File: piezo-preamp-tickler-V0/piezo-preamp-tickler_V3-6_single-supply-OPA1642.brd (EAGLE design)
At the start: 100.3 x 20.1 mm, 58 parts, among them IC1 OPA1642, IC2 DMN2400, IC3 BQ21040, IC4 BQ297X, IC5 SC4503, IC6 TPS7A49, J1 HEADPHONES, J2 PHONE, J3 Mixer, J5 Battery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

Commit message: Add files via upload
DRC issues fixed for previous changes
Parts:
- moved R19 2.51 mm to (51.9, 14.0)
- moved R17 2.20 mm to (52.0, 11.0)
- moved CN1 0.32 mm to (38.1, 16.7)
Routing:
- net N$30: track 120.0 -> 115.6 mm
- net V+: track 114.5 -> 117.4 mm
- net N$28: track 63.3 -> 65.4 mm
- net N$17: track 100.4 -> 101.9 mm
- net GND: track 177.1 -> 178.5 mm
- net N$29: track 53.2 -> 52.0 mm

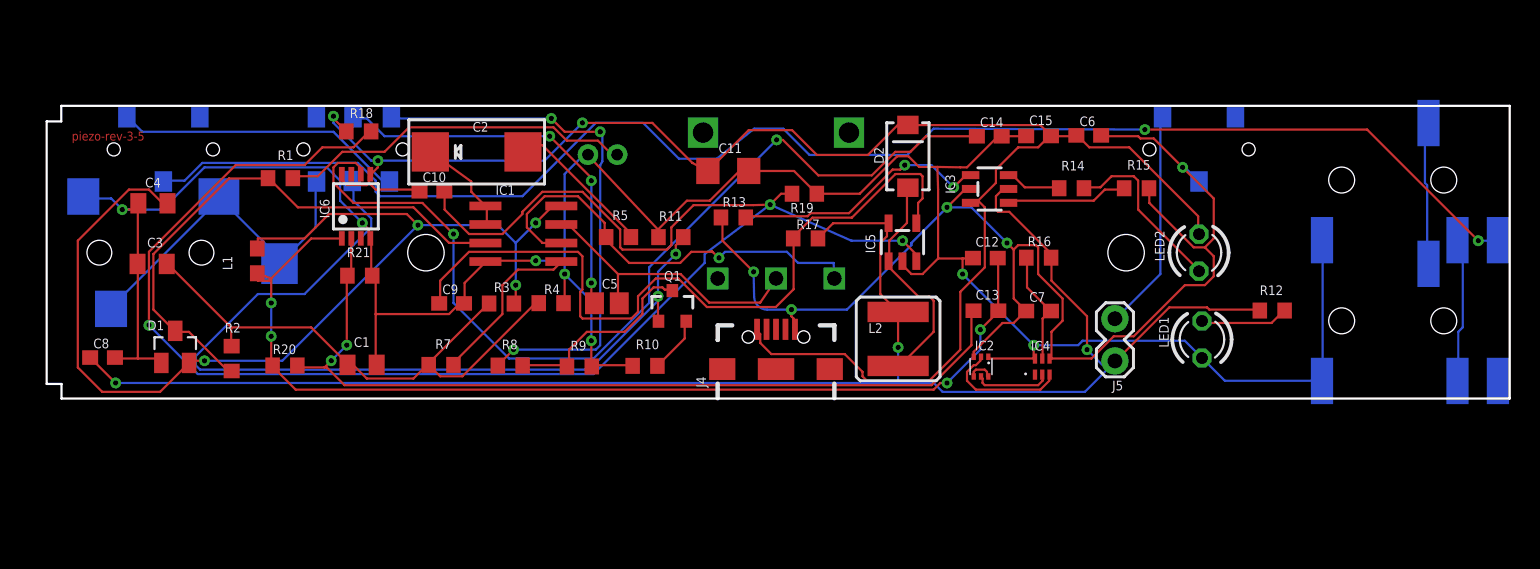
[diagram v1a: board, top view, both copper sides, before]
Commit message: issues 14 and 17 resolved
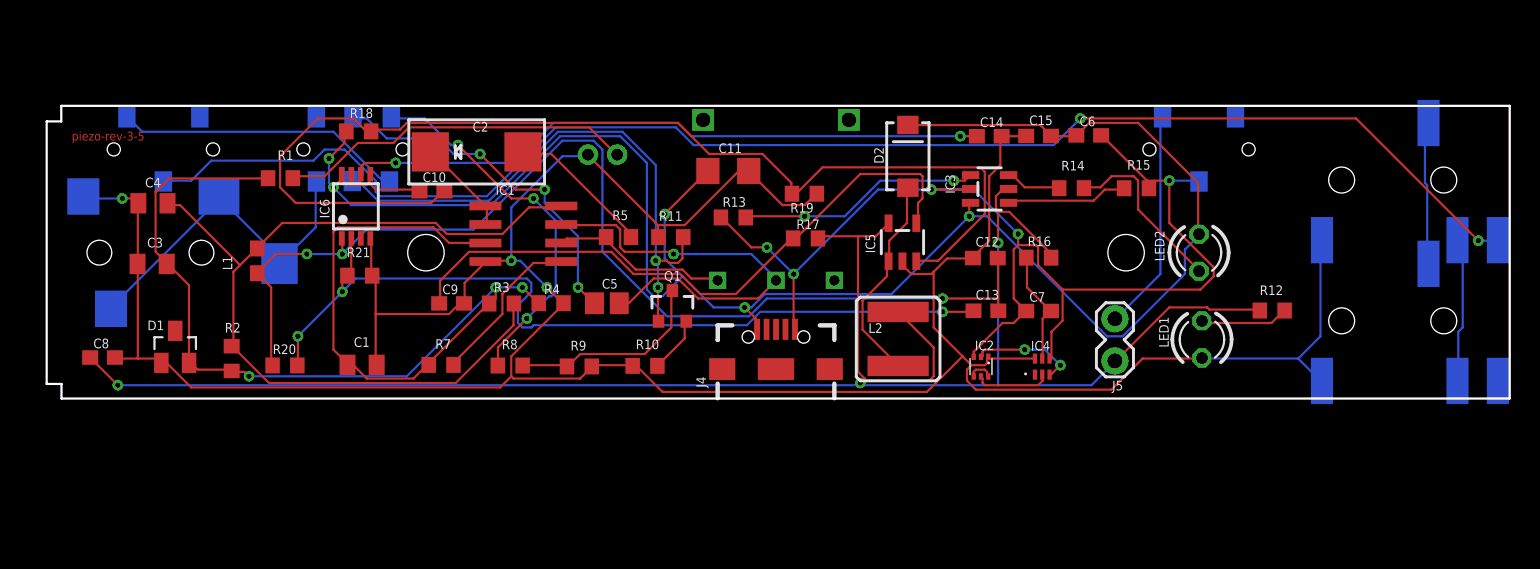
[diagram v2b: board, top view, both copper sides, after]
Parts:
- removed R6: 50K, CMU-ArtFab:THUMBPOT14MM
- added U$1: PIEZO-PREAMP-TICKLER_V3-5_SINGLE-SUPPLY-OPA1642_50K_DIAL_POT, custom_packages:PIEZO-PREAMP-TICKLER_V3-5_SINGLE-SUPPLY-OPA1642_50K_DIAL_POT
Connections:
- removed net N$23: C1.1, C3.1, R2.1, R3.1, R4.2, R7.2
- removed net N$25: C4.1, D1.2, IC1.8, L1.2, R3.2
- removed net N$9: D1.3, IC1.3, R1.2, R2.2
- new net N$1: C1.1, C3.1, D1.2, IC1.3, R1.2, R2.2, R3.1, R4.2, R7.2
- new net N$8: C4.1, IC1.8, L1.2, R2.1, R3.2
- net N$6: now also U$1.2; no longer R6.P$2
- net N$7: now also U$1.1; no longer R6.P$1
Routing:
- net N$1: track 0.00 -> 82.3 mm, vias 0 -> 3
- net N$25: track 73.7 -> 0.00 mm, vias 4 -> 0
- net N$8: track 0.00 -> 60.4 mm
- net N$30: track 115.6 -> 76.4 mm, vias 3 -> 0
- net N$23: track 38.9 -> 0.00 mm
- net N$9: track 37.7 -> 0.00 mm
- net GND: track 178.5 -> 204.9 mm, vias 7 -> 3
- net SELECT: track 60.6 -> 38.6 mm
- net N$28: track 65.4 -> 44.4 mm
- net N$7: track 30.0 -> 12.2 mm, vias 1 -> 0
- net V+: track 117.4 -> 132.9 mm, vias 3 -> 5
- net N$11: track 37.0 -> 25.9 mm
- net VBAT: track 118.1 -> 128.7 mm
- net N$6: track 19.9 -> 29.6 mm, vias 0 -> 1
- net N$29: track 52.0 -> 43.7 mm
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
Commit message: Custom device added for 50K pot
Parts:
- U$1: device custom_packages:PIEZO-PREAMP-TICKLER_V3-5_SINGLE-SUPPLY-OPA1642_50K_DIAL_POT -> CMU-ArtFab:PIEZO-PREAMP-TICKLER_V3-5_SINGLE-SUPPLY-OPA1642_50K_DIAL_POT
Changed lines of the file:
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@@
 <attribute name="VALUE" x="69.175" y="17.175" size="0.6604" layer="27" font="vector" ratio="15" rot="R180"/>
 </element>
-<element name="U$1" library="custom_packages" package="PIEZO-PREAMP-TICKLER_V3-5_SINGLE-SUPPLY-OPA1642_50K_DIAL_POT" value="PIEZO-PREAMP-TICKLER_V3-5_SINGLE-SUPPLY-OPA1642_50K_DIAL_POT" x="50" y="16.1"/>
+<element name="U$1" library="CMU-ArtFab" package="PIEZO-PREAMP-TICKLER_V3-5_SINGLE-SUPPLY-OPA1642_50K_DIAL_POT" value="PIEZO-PREAMP-TICKLER_V3-5_SINGLE-SUPPLY-OPA1642_50K_DIAL_POT" x="50" y="16.1"/>
 </elements>
 <signals>

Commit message: issue #18 solved
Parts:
- R20: value 91.2k -> 100k
- R21: value 100k -> 11k
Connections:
- net N$12: now also SW1.6; no longer SW1.3
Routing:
- net V+: track 132.9 -> 99.0 mm
- net N$19: track 19.8 -> 43.0 mm
- net N$17: track 100.9 -> 119.0 mm
- net GND2: track 80.9 -> 98.4 mm, vias 5 -> 3
- net N$1: track 82.3 -> 66.1 mm
- net N$28: track 44.4 -> 58.8 mm, vias 2 -> 0
- net N$30: track 76.4 -> 64.6 mm, vias 0 -> 2
- net GND: track 204.9 -> 213.0 mm, vias 3 -> 2
- net N$6: track 29.6 -> 22.0 mm, vias 1 -> 0
- net +12V: track 75.7 -> 68.3 mm, vias 3 -> 2
- net SELECT: track 38.6 -> 31.3 mm, vias 2 -> 4
- net N$11: track 25.9 -> 29.8 mm
- net VBAT: track 128.7 -> 132.0 mm
- net N$12: track 23.8 -> 26.3 mm
- net N$26: track 58.6 -> 56.2 mm, vias 3 -> 2
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
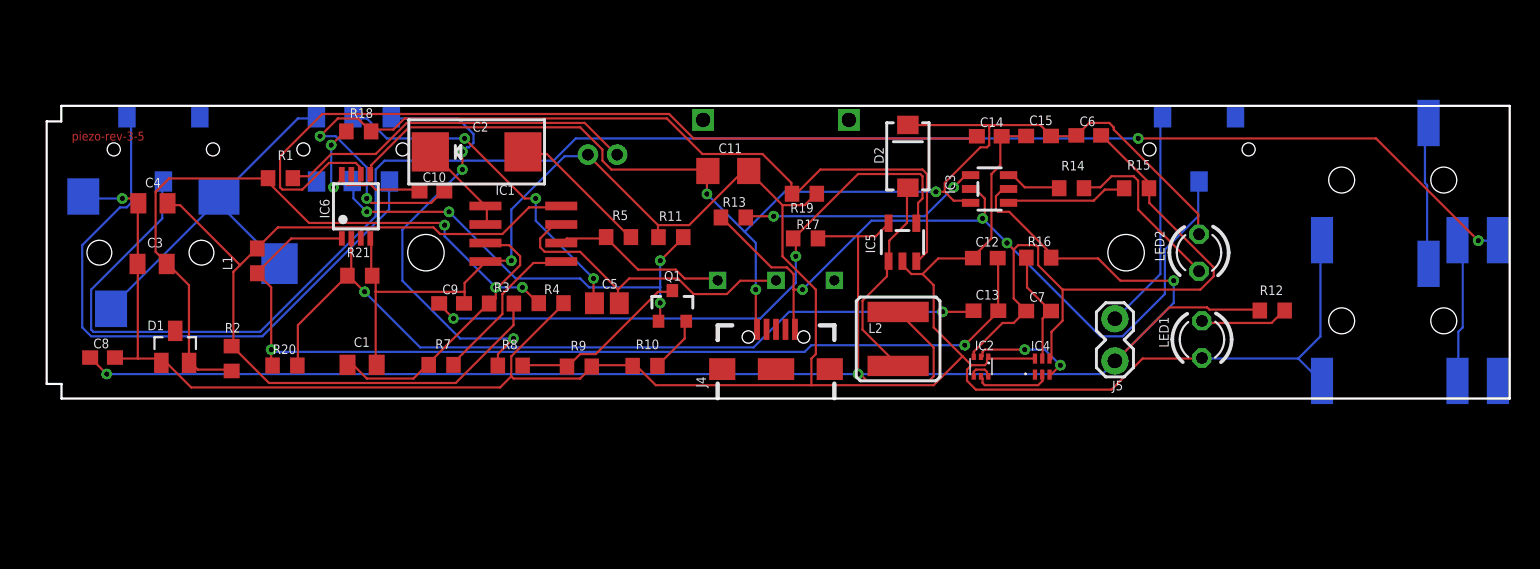
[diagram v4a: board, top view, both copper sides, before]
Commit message: Issues 17 and 19 fixed
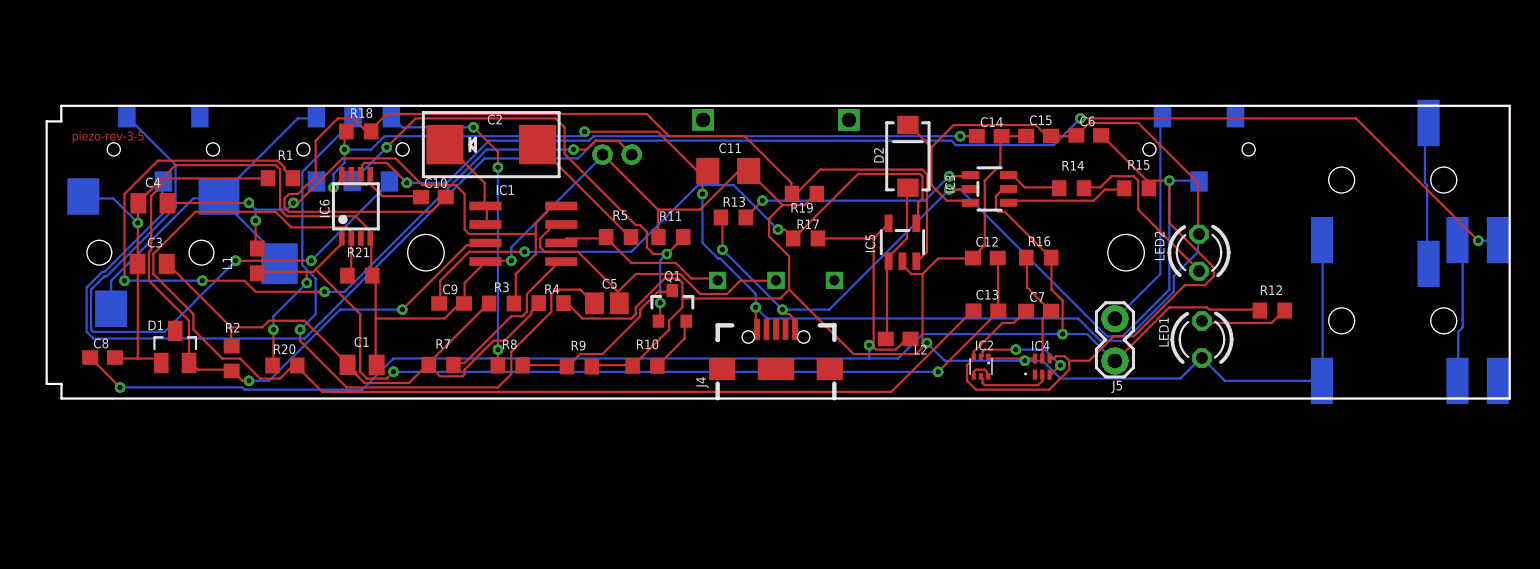
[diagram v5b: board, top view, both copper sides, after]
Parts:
- L2: device SparkFun-Passives:CR54 -> SparkFun-Passives:0603
- moved C2 1.12 mm to (30.5, 17.4)
- moved CN1 1.00 mm to (39.1, 16.7)
- moved C10 0.41 mm to (26.5, 13.8)
- turned L2 to 180 degrees
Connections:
- new net N$9: C1.1, C3.1, R2.1, R3.1, R4.2, R7.2
- net N$1: no longer C1.1, C3.1, R3.1, R4.2, R7.2
- net N$32: now also L2.2; no longer L2.P$2
- net N$8: no longer R2.1
- net VBAT: now also L2.1; no longer L2.P$1
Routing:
- net N$9: track 0.00 -> 39.9 mm
- net N$2: track 24.7 -> 58.8 mm, vias 0 -> 4
- net N$26: track 56.2 -> 83.1 mm, vias 2 -> 0
- net V+: track 99.0 -> 120.5 mm
- net N$1: track 66.1 -> 45.9 mm, vias 3 -> 2
- net N$16: track 23.7 -> 43.9 mm, vias 3 -> 1
- net N$8: track 60.1 -> 41.6 mm, vias 0 -> 3
- net VBAT: track 132.0 -> 114.6 mm
- net N$28: track 58.8 -> 44.8 mm, vias 0 -> 2
- net GND: track 213.0 -> 200.7 mm, vias 2 -> 4
- net N$11: track 29.8 -> 22.9 mm
- net N$30: track 64.6 -> 70.7 mm, vias 2 -> 0
- net SELECT: track 31.3 -> 35.4 mm, vias 4 -> 3
- net +12V: track 68.3 -> 72.3 mm, vias 2 -> 4
- net N$32: track 14.5 -> 11.0 mm
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
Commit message: Bug in issue #23 fixed
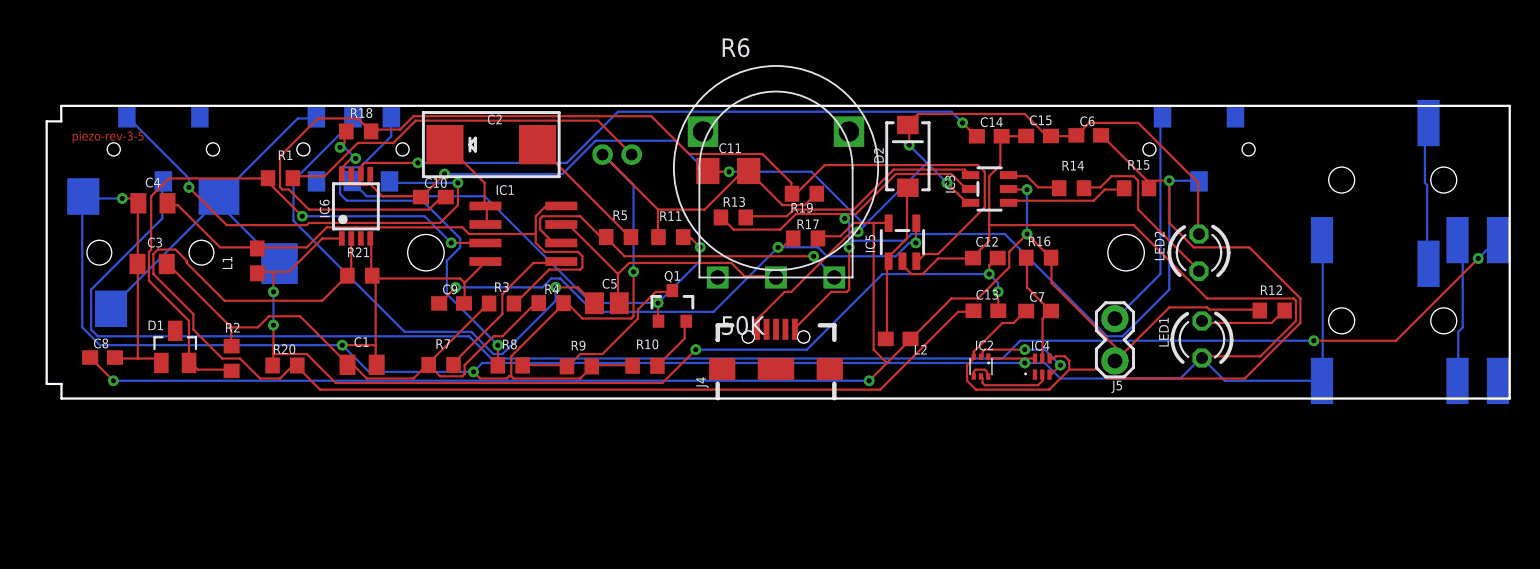
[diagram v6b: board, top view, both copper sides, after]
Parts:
- removed U$1: PIEZO-PREAMP-TICKLER_V3-5_SINGLE-SUPPLY-OPA1642_50K_DIAL_POT, CMU-ArtFab:PIEZO-PREAMP-TICKLER_V3-5_SINGLE-SUPPLY-OPA1642_50K_DIAL_POT
- added R6: 50K, CMU-ArtFab:THUMBPOT14MM
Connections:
- net N$6: now also R6.P$2; no longer U$1.2
- net N$7: now also R6.P$3; no longer U$1.1
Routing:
- net GND: track 200.7 -> 254.4 mm, vias 4 -> 5
- net N$2: track 58.8 -> 25.9 mm, vias 4 -> 0
- net V+: track 120.5 -> 97.9 mm, vias 5 -> 7
- net GND2: track 100.4 -> 122.9 mm, vias 4 -> 3
- net N$7: track 12.1 -> 24.6 mm, vias 0 -> 1
- net N$19: track 43.3 -> 32.9 mm
- net N$16: track 43.9 -> 36.1 mm
- net N$17: track 119.5 -> 112.8 mm
- net N$30: track 70.7 -> 77.0 mm
- net N$29: track 44.2 -> 39.4 mm, vias 2 -> 3
- net N$11: track 22.9 -> 27.6 mm, vias 3 -> 1
- net N$1: track 45.9 -> 41.5 mm
- net N$6: track 22.2 -> 19.0 mm
- net SELECT: track 35.4 -> 32.2 mm, vias 3 -> 2
- net VBAT: track 114.6 -> 112.5 mm, vias 3 -> 4
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
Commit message: Add files via upload
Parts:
- moved C2 0.30 mm to (30.8, 17.4)
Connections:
- net N$4: now also SW2.P$3
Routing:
- net N$4: track 0.00 -> 116.0 mm, vias 0 -> 4
- net VBAT: track 112.5 -> 151.1 mm, vias 4 -> 1
- net GND2: track 122.9 -> 91.8 mm, vias 3 -> 5
- net V+: track 97.9 -> 120.0 mm, vias 7 -> 6
- net SELECT: track 32.2 -> 47.6 mm, vias 2 -> 6
- net N$17: track 112.8 -> 127.3 mm
- net N$19: track 32.9 -> 46.3 mm
- net GND: track 254.4 -> 247.4 mm, vias 5 -> 6
- net N$11: track 27.6 -> 21.7 mm, vias 1 -> 3
- net N$29: track 39.4 -> 45.1 mm, vias 3 -> 4
- net +12V: track 70.4 -> 75.7 mm
- net N$16: track 36.1 -> 33.7 mm, vias 1 -> 3
- net N$8: track 41.3 -> 42.8 mm
- net N$30: track 77.0 -> 78.4 mm
- net N$28: track 45.1 -> 46.1 mm
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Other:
- board text added: "HEADSET"
- board text added: "MIXER"
- board text added: "OFF"
- board text added: "ON"
- board text added: "PHONE"
- board text added: "PIEZO"
- board text added: "piezo-rev-3-6"
- board text removed: "piezo-rev-3-5"

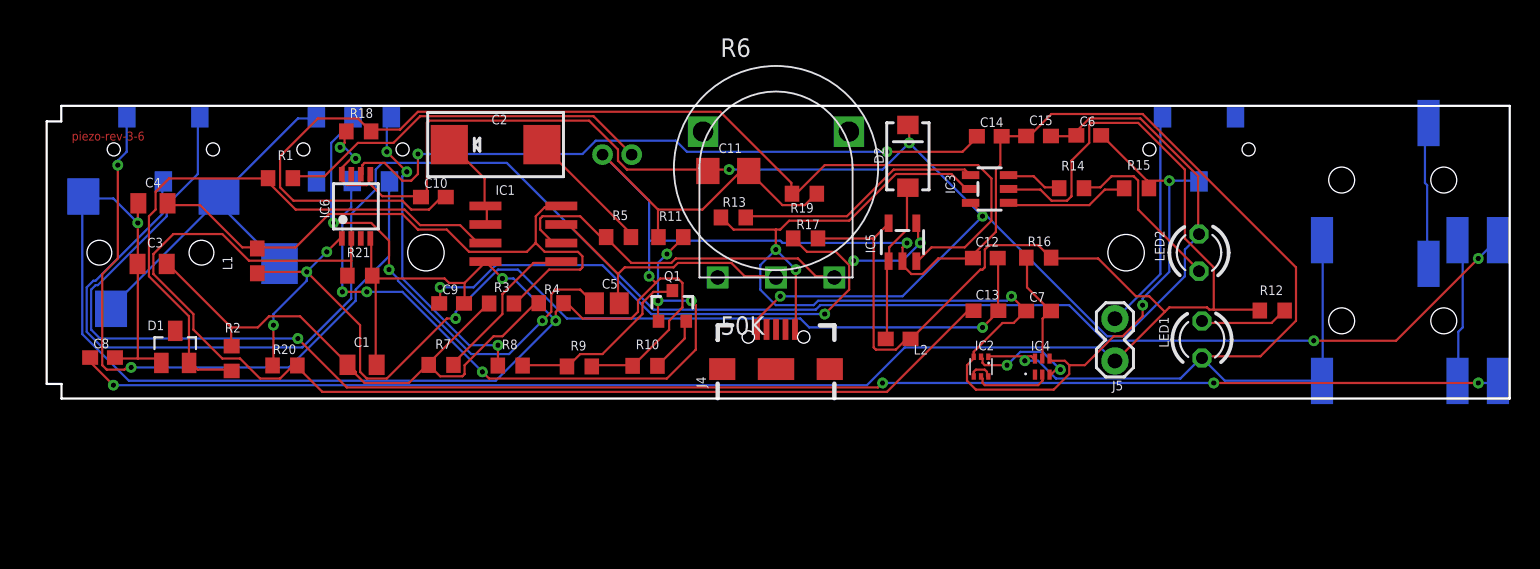
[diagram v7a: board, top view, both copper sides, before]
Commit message: updated charging and footprints
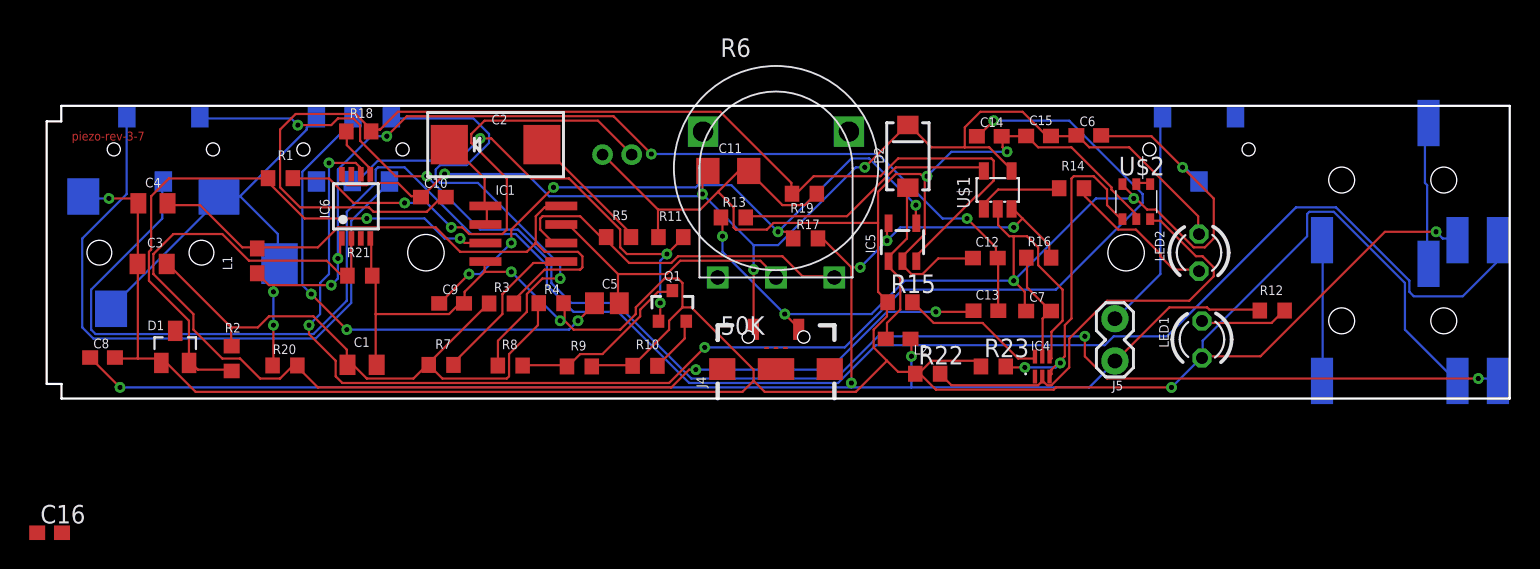
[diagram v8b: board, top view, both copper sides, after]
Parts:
- removed IC2: DMN2400, CMU-ArtFab:SOT-563
- removed IC3: BQ21040, CMU-ArtFab:SOT23-6
- added C16: 4.7uF, rcl:C0603
- added R22, R23: 10M, CMU-ArtFab:R0603
- added U$1: MCP73831, CMU-ArtFab:SOT-23-5
- added U$2: QS6K1, CMU-ArtFab:SOT457R_PHILIPS
- C6: value 10uF -> 4.7uF
- IC4: device CMU-ArtFab:WSON-6 -> CMU-ArtFab:WSON-6-LONG
- J4: device SparkFun-Connectors:USB-B-MICRO-SMD_RED_PASTE -> CMU-ArtFab:USB-B-MICRO-SMD_RED_PASTE
- R13: value 10k -> 5k
- R14: value 1k -> 470
- R15: value 10k -> 2.2k
- moved R15 18.0 mm to (58.5, 6.60), turned to 0 degrees
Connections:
- removed net GND2: C6.2, C7.1, IC2.3, IC3.5, IC4.4, J4.GND, R13.1, R15.1, SW3.P$2
- removed net N$15: J1.RING2, J2.RING2
- removed net N$20: J5.2, SW3.P$1
- removed net N$36: IC3.4, R13.2
- removed net N$43: IC2.4, IC2.6
- removed net N$44: IC2.5, IC4.2
- removed net N$45: IC2.2, IC4.3
- new net BATGND: C7.1, IC4.4, SW3.P$2, U$2.6
- new net N$21: R13.2, U$1.5
- new net N$23: U$2.4, U$2.5
- new net N$25: R14.2, U$1.1
- new net N$33: J1.TIP, J2.TIP
- new net N$34: IC4.6, R15.2
- new net USBGND: C16.2, C6.2, J4.GND, J5.2, R13.1, SW3.P$1, U$1.2
- net GND: now also J1.RING2, J2.RING2, R15.1, R22.1, R23.1, U$2.2; no longer IC2.1, IC4.6, J1.TIP, J2.TIP
- net N$27: now also IC4.3, R23.2, U$2.1; no longer IC3.3, R14.2
- net N$31: now also IC4.2, R22.2, U$2.3; no longer IC3.1, R15.2
- net V+: now also U$1.4; no longer IC3.6
- net VBAT: now also C16.1, U$1.3; no longer IC3.2
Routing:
- net GND2: track 91.8 -> 0.00 mm, vias 5 -> 0
- net BATGND: track 0.00 -> 77.7 mm, vias 0 -> 5
- net N$28: track 46.1 -> 93.8 mm, vias 2 -> 4
- net GND: track 247.4 -> 285.9 mm, vias 6 -> 7
- net VBAT: track 151.1 -> 117.0 mm, vias 1 -> 6
- net V+: track 120.0 -> 88.5 mm, vias 6 -> 4
- net N$31: track 8.46 -> 30.3 mm
- net N$27: track 3.85 -> 23.6 mm, vias 0 -> 2
- net N$21: track 0.00 -> 17.9 mm
- net N$36: track 16.9 -> 0.00 mm
- net USBGND: track 0.00 -> 15.2 mm
- net N$20: track 15.2 -> 0.00 mm
- net N$4: track 116.0 -> 101.5 mm
- net SELECT: track 47.6 -> 33.3 mm, vias 6 -> 3
- net N$11: track 21.7 -> 33.2 mm, vias 3 -> 1
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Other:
- board text added: "piezo-rev-3-7"
- board text removed: "piezo-rev-3-6"
